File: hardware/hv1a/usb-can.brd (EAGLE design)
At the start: 30 x 22 mm, 26 parts, among them CON1 2EDG-4P, U1 MCP2515-ML, U2 MCP2562-MF, U3 CP2130

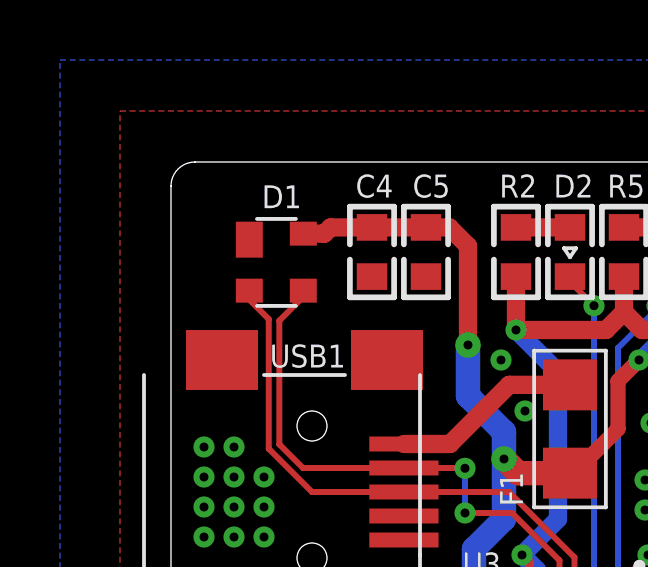
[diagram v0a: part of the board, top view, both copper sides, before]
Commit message: Add more vias and generate gerbers
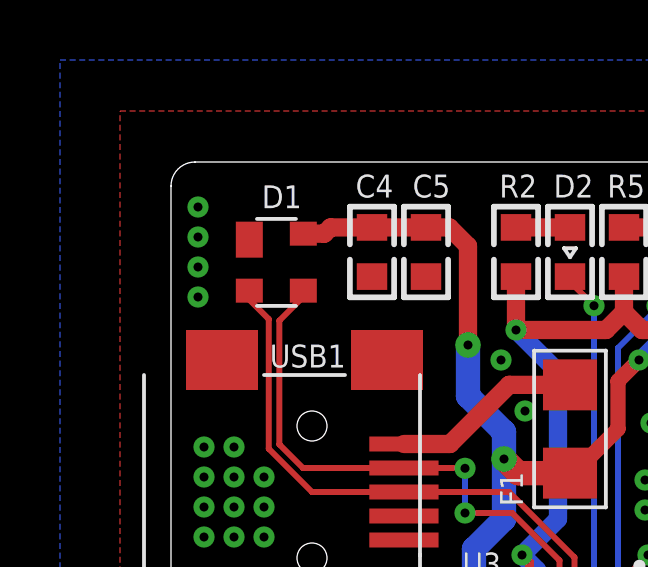
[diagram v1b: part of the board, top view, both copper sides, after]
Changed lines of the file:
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@@
 </class>
 </classes>
-<designrules name="mask_vias">
+<designrules name="default">
 <description language="de">&lt;b&gt;EAGLE Design Rules&lt;/b&gt;
 &lt;p&gt;
@@
 <param name="mdViaViaSameLayer" value="6mil"/>
 <param name="mnLayersViaInSmd" value="2"/>
-<param name="mdCopperDimension" value="16mil"/>
+<param name="mdCopperDimension" value="0.2mm"/>
 <param name="mdDrill" value="6mil"/>
 <param name="mdSmdStop" value="0mil"/>
@@
 <via x="28.1" y="15.6" extent="1-16" drill="0.3"/>
 <via x="11.8" y="13.7" extent="1-16" drill="0.3"/>
+<via x="0.9" y="20.5" extent="1-16" drill="0.3"/>
+<via x="0.9" y="19.5" extent="1-16" drill="0.3"/>
+<via x="0.9" y="18.5" extent="1-16" drill="0.3"/>
+<via x="0.9" y="17.5" extent="1-16" drill="0.3"/>
+<wire x1="0.9" y1="17.5" x2="0.9" y2="18.5" width="0" layer="19" extent="1-1"/>
+<wire x1="0.9" y1="19.5" x2="0.9" y2="18.5" width="0" layer="19" extent="1-1"/>
 </signal>
 <signal name="!CS">
